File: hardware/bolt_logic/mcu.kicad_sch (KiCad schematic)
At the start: 24 parts, among them J1 SWD, U3 STM32F103RBT6, Y1 8MHz, Y2 32.768kHz

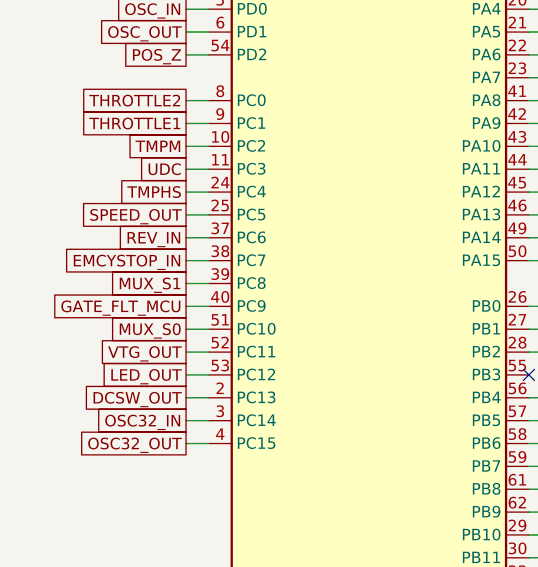
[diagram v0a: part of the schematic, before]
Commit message: Remove the aux header (J3) and V6 leftovers: only CN1, CN2 and programming
Owner: the only connections on the board are CN1, CN2 and what is needed
to program it (J1 SWD, J4 ESP32).

- Removed J3 and what only served it: aux 12 V / 5 V outputs (F3, F4),
  aux temperature pull-up and filter (R56, C67; mux 1Y1 grounded), the
  emergency-stop / motor-protection header resistors and caps (R110,
  R112, C105, C106; the 10k pull-ups stay, so the firmware reads OK).
- CN1 G1/G2 (HVIL) only went to J3: now reserved positions.
- PC11 (VTG_OUT) and PC5 (SPEED_OUT, never connected) now NC.
- Re-placed and re-routed: 241 parts, DRC 0 violations, 0 unconnected.
- Docs: 03 (pin map, 4.10, 4.12, 4.13, CN1 table), 04, 05 updated;
  SWD header described as the 5-pin part it is.

Co-Authored-By: Claude Opus 5.5 <noreply@anthropic.com>
Claude-Session: https://claude.ai/code/session_01KW1M8KfVLc83FDDiK2YEWM
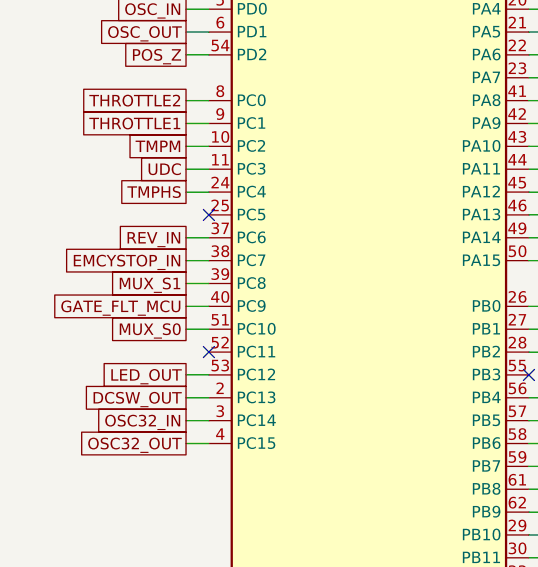
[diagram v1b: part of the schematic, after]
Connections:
- net SPEED_OUT: no longer names the net of U3.25 (PC5)
- net VTG_OUT: no longer names the net of U3.52 (PC11)
- no-connect marks 1 -> 3
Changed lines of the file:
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@@
       (effects
         (font (size 1.27 1.27)) hide)))
-  (wire
-    (pts
-      (xy 33.02 76.2)
-      (xy 30.48 76.2))
-    (stroke
-      (width 0)
-      (type default))
-)
-  (global_label "SPEED_OUT"
-    (shape passive)
-    (at 30.48 76.2 180)
-    (fields_autoplaced)
-    (effects
-      (font (size 1.27 1.27))
-      (justify right))
-    (property "Intersheetrefs" "${INTERSHEET_REFS}"
-      (at 30.48 76.2 0)
-      (effects
-        (font (size 1.27 1.27)) hide)))
+  (no_connect
+    (at 33.02 76.2)
+)
   (wire
     (pts
@@
       (effects
         (font (size 1.27 1.27)) hide)))
-  (wire
-    (pts
-      (xy 33.02 91.44)
-      (xy 30.48 91.44))
-    (stroke
-      (width 0)
-      (type default))
-)
-  (global_label "VTG_OUT"
-    (shape passive)
-    (at 30.48 91.44 180)
-    (fields_autoplaced)
-    (effects
-      (font (size 1.27 1.27))
-      (justify right))
-    (property "Intersheetrefs" "${INTERSHEET_REFS}"
-      (at 30.48 91.44 0)
-      (effects
-        (font (size 1.27 1.27)) hide)))
-  (wire
-    (pts
+  (no_connect
+    (at 33.02 91.44)
+)
+  (wire
+    (pts
